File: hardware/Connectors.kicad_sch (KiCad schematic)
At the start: 2 parts, among them J2 Conn_02x20_Odd_Even, U1 AS222-35PN-933

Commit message: minor improvements
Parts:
- added C25: 10pF, Capacitor_SMD:CP_Elec_6.3x7.7, symbol Device:CP_Small
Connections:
- net +24V: now also U1.27, U1.37
- net +5V: now also C25.1
- net AMS: now also U1.31; no longer U1.75
- net BREAK_LIGHT_IN: now also U1.74; no longer U1.93
- net GND: now also U1.10, U1.11, U1.12, U1.13, U1.33, U1.4, U1.44, U1.48, U1.54, U1.75, U1.81, U1.82, U1.83, U1.84, U1.9, C25.2
- net HVD: now also U1.42; no longer U1.74
- net SPARE: now also U1.43; no longer U1.66
- net TD: now also U1.53; no longer U1.76
- net TSMS: now also U1.32; no longer U1.65
- net V_PUMP: now also U1.64, U1.65, U1.66; no longer U1.83, U1.84, U1.85
- new net V_SPARE_1: U1.93
- new net V_SPARE_2: U1.85
- new net V_SPARE_3: U1.76
- no-connect marks 24 -> 5

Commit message: fuck
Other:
- note added: "res ref do wyjbania"
- note added: "ws_rr/rl/fr/fl do wyjbania na jeden"
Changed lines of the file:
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@@
     (effects (font (size 2.9972 2.9972) (thickness 0.5994) bold) (justify right bottom))
+  )
+  (text "ws_rr/rl/fr/fl do wyjbania na jeden" (at -5.08 62.23 0)
+    (effects (font (size 1.27 1.27)) (justify left bottom))
+  )
+  (text "res ref do wyjbania\n" (at 76.2 125.73 0)
+    (effects (font (size 1.27 1.27)) (justify left bottom))
   )
   (text "BUS" (at 136.652 72.39 180)

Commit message: jolo
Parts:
- U1: footprint AS222-35PN-933C:AS222-35PN-933C-ver3-drill_0.72_size_1.02 -> Autosport:AS222-35PN-933C-ver4-drill_0.72_size_1.02
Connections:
- net GND: no longer U1.10, U1.11, U1.12, U1.13, U1.4, U1.9
- net USB_DM: no longer U1.17
- net USB_DP: no longer U1.16
- net DASHBOARD renamed ODRIVE
- net ODRIVE: now also U1.10, U1.9
- net JETSON_??? renamed JETSON
- net WS_RL renamed LAPTIMER
- net WS_RR renamed DASH
- new net TSAL_HV_AIR: U1.16
- new net TSAL_HV_SIG: U1.17
- new net TSAL_LED_GREEN: U1.4
- new net TSAL_LED_HV: U1.12
- new net TSAL_LED_LV: U1.13
- new net TSAL_LED_RED: U1.11

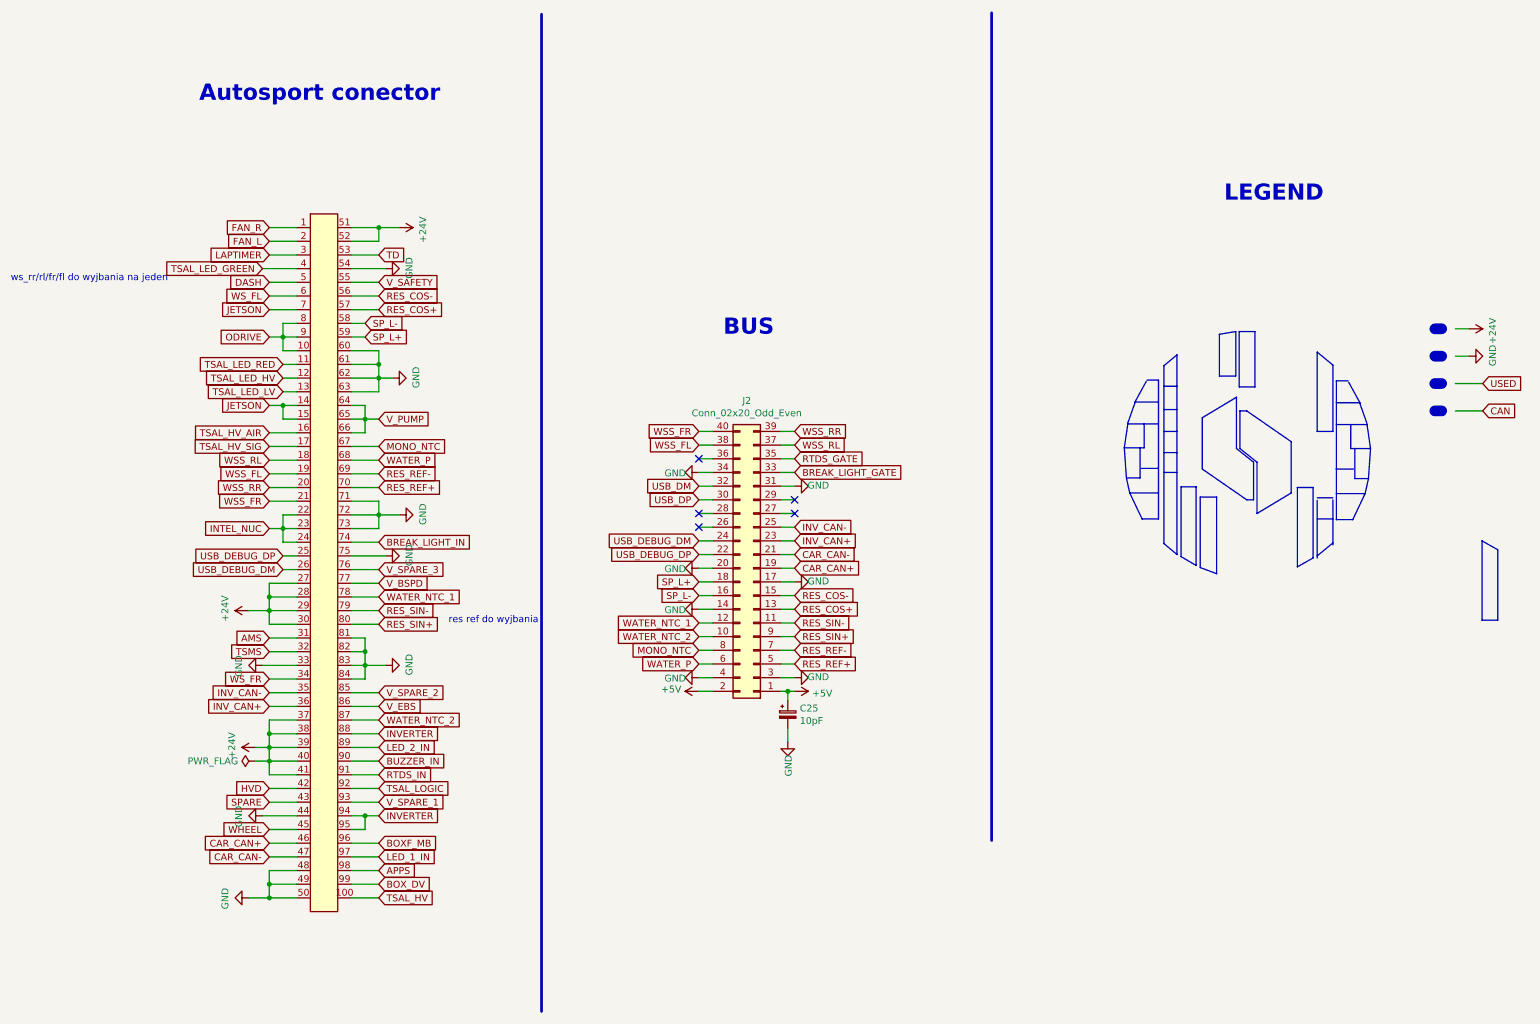
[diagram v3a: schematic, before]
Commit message: currected sf autosport connector, also updated firmware to better handle the showing of board status throught the on board LEDs
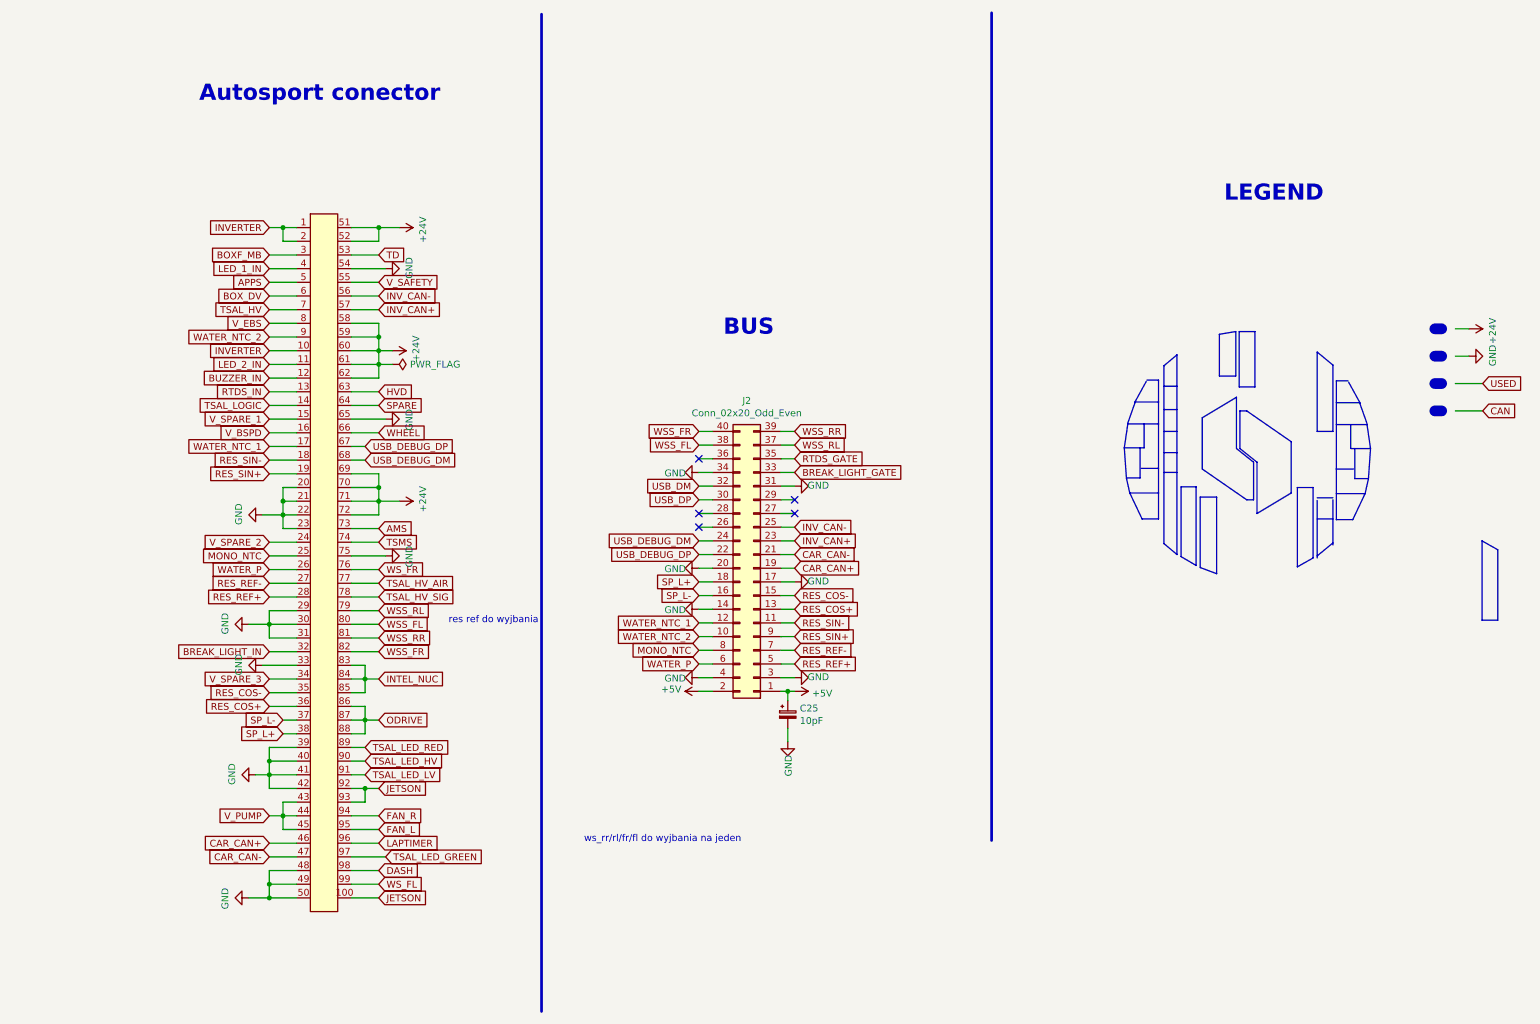
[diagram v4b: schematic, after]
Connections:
- net +24V: now also U1.58, U1.59, U1.60, U1.61, U1.62, U1.69, U1.70, U1.71, U1.72; no longer U1.27, U1.28, U1.29, U1.30, U1.37, U1.38, U1.39, U1.40, U1.41
- net AMS: now also U1.73; no longer U1.31
- net APPS: now also U1.5; no longer U1.98
- net BOXF_MB: now also U1.3; no longer U1.96
- net BOX_DV: now also U1.6; no longer U1.99
- net BREAK_LIGHT_IN: now also U1.32; no longer U1.74
- net BUZZER_IN: now also U1.12; no longer U1.90
- net DASH: now also U1.98; no longer U1.5
- net FAN_L: now also U1.95; no longer U1.2
- net FAN_R: now also U1.94; no longer U1.1
- net GND: now also U1.20, U1.21, U1.22, U1.23, U1.29, U1.30, U1.31, U1.39, U1.40, U1.41, U1.42, U1.65; no longer U1.44, U1.60, U1.61, U1.62, U1.63, U1.71, U1.72, U1.73, U1.81, U1.82, U1.83, U1.84
- net HVD: now also U1.63; no longer U1.42
- net INTEL_NUC: now also U1.83, U1.84, U1.85; no longer U1.22, U1.23, U1.24
- net INVERTER: now also U1.1, U1.10, U1.2; no longer U1.88, U1.94, U1.95
- net INV_CAN+: now also U1.57; no longer U1.36
- net INV_CAN-: now also U1.56; no longer U1.35
- net JETSON: now also U1.100, U1.92, U1.93; no longer U1.14, U1.15, U1.7
- net LAPTIMER: now also U1.96; no longer U1.3
- net LED_1_IN: now also U1.4; no longer U1.97
- net LED_2_IN: now also U1.11; no longer U1.89
- net MONO_NTC: now also U1.25; no longer U1.67
- net ODRIVE: now also U1.86, U1.87, U1.88; no longer U1.10, U1.8, U1.9
- net RES_COS+: now also U1.36; no longer U1.57
- net RES_COS-: now also U1.35; no longer U1.56
- net RES_REF+: now also U1.28; no longer U1.70
- net RES_REF-: now also U1.27; no longer U1.69
- net RES_SIN+: now also U1.19; no longer U1.80
- net RES_SIN-: now also U1.18; no longer U1.79
- net RTDS_IN: now also U1.13; no longer U1.91
- net SPARE: now also U1.64; no longer U1.43
- net SP_L+: now also U1.38; no longer U1.59
- net SP_L-: now also U1.37; no longer U1.58
- net TSAL_HV: now also U1.7; no longer U1.100
- net TSAL_HV_AIR: now also U1.77; no longer U1.16
- net TSAL_HV_SIG: now also U1.78; no longer U1.17
- net TSAL_LED_GREEN: now also U1.97; no longer U1.4
- net TSAL_LED_HV: now also U1.90; no longer U1.12
- net TSAL_LED_LV: now also U1.91; no longer U1.13
- net TSAL_LED_RED: now also U1.89; no longer U1.11
- net TSAL_LOGIC: now also U1.14; no longer U1.92
- net TSMS: now also U1.74; no longer U1.32
- net USB_DEBUG_DM: now also U1.68; no longer U1.26
- net USB_DEBUG_DP: now also U1.67; no longer U1.25
- net V_BSPD: now also U1.16; no longer U1.77
- net V_EBS: now also U1.8; no longer U1.86
- net V_PUMP: now also U1.43, U1.44, U1.45; no longer U1.64, U1.65, U1.66
- net V_SPARE_1: now also U1.15; no longer U1.93
- net V_SPARE_2: now also U1.24; no longer U1.85
- net V_SPARE_3: now also U1.34; no longer U1.76
- net WATER_NTC_1: now also U1.17; no longer U1.78
- net WATER_NTC_2: now also U1.9; no longer U1.87
- net WATER_P: now also U1.26; no longer U1.68
- net WHEEL: now also U1.66; no longer U1.45
- net WSS_FL: now also U1.80; no longer U1.19
- net WSS_FR: now also U1.82; no longer U1.21
- net WSS_RL: now also U1.79; no longer U1.18
- net WSS_RR: now also U1.81; no longer U1.20
- net WS_FL: now also U1.99; no longer U1.6
- net WS_FR: now also U1.76; no longer U1.34

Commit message: major schematic update, changed optocouplers for different, added new fuses for 5v supply for water and potentiometers and 24v supply for BSPD/ESB, updated autosport connector, and some other changes
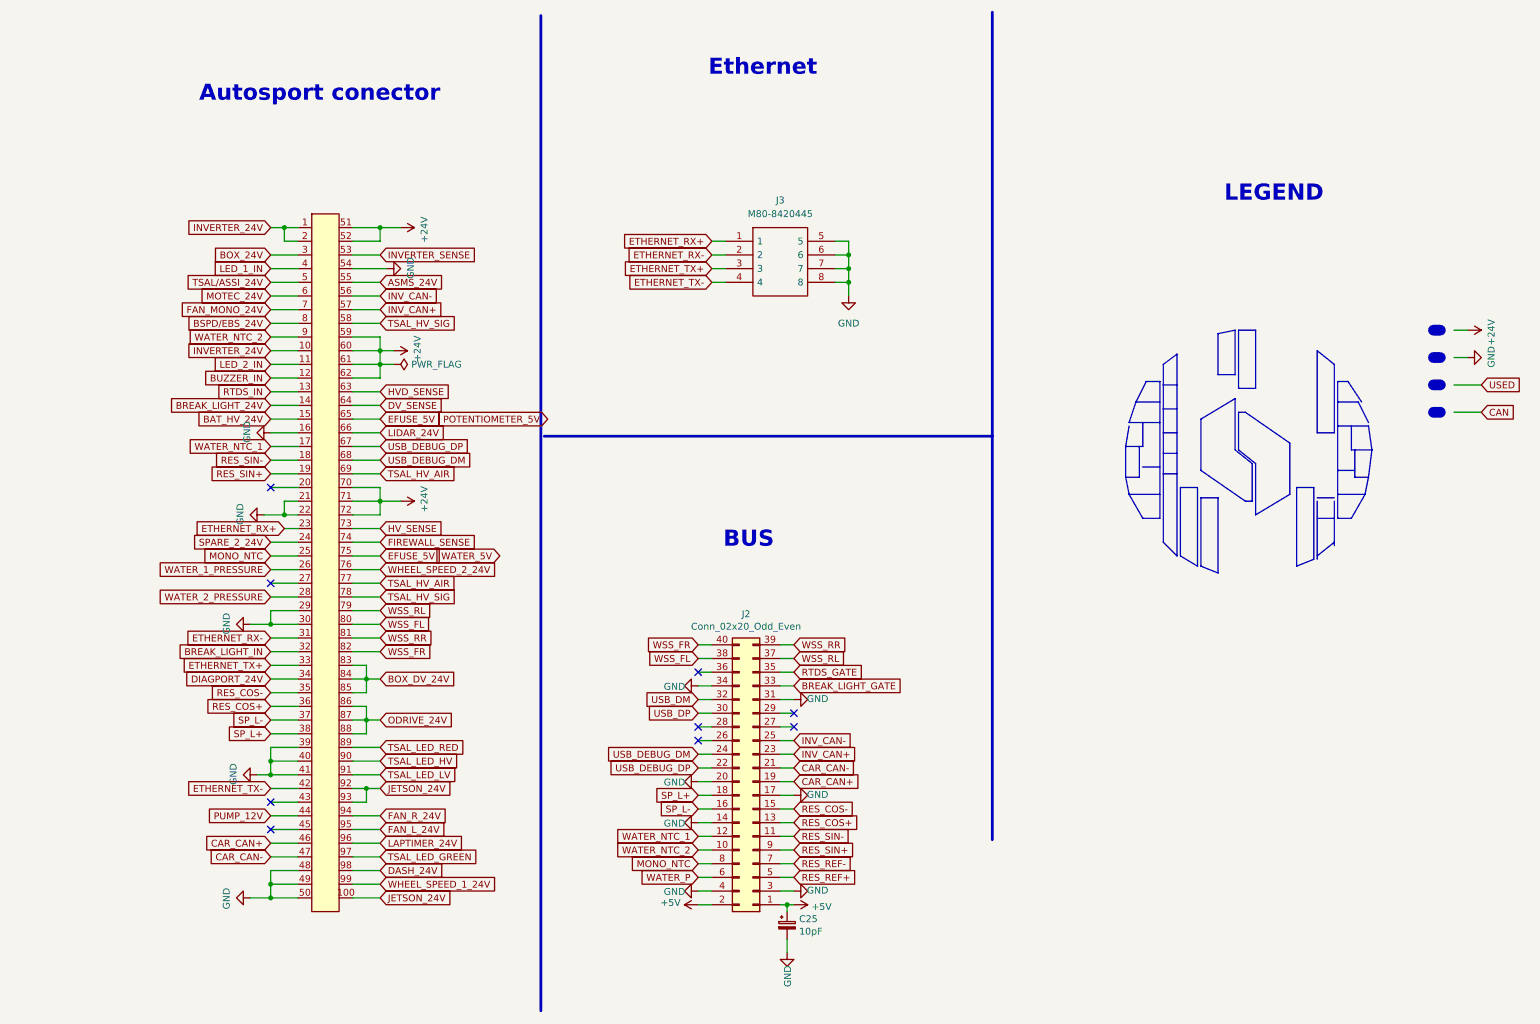
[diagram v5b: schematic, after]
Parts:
- added J3: M80-8420445, M80-8420445, symbol M80-8420445:M80-8420445
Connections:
- net V_BSPD is gone; now on net GND: U1.16
- net +24V: no longer U1.58, U1.69
- net GND: now also J3.5, J3.6, J3.7, J3.8; no longer U1.20, U1.23, U1.31, U1.33, U1.42, U1.65, U1.75
- net RES_REF+: no longer U1.28
- net RES_REF-: no longer U1.27
- net TSAL_HV_AIR: now also U1.69
- net TSAL_HV_SIG: now also U1.58
- net WATER_P: no longer U1.26
- net AMS renamed HV_SENSE
- net APPS renamed TSAL/ASSI_24V
- net BOXF_MB renamed BOX_24V
- net BOX_DV renamed MOTEC_24V
- net DASH renamed DASH_24V
- net FAN_L renamed FAN_L_24V
- net FAN_R renamed FAN_R_24V
- net HVD renamed HVD_SENSE
- net INTEL_NUC renamed BOX_DV_24V
- net INVERTER renamed INVERTER_24V
- net JETSON renamed JETSON_24V
- net LAPTIMER renamed LAPTIMER_24V
- net ODRIVE renamed ODRIVE_24V
- net SPARE renamed DV_SENSE
- net TD renamed INVERTER_SENSE
- net TSAL_HV renamed FAN_MONO_24V
- net TSAL_LOGIC renamed BREAK_LIGHT_24V
- net TSMS renamed FIREWALL_SENSE
- net V_EBS renamed BSPD/EBS_24V
- removed net V_PUMP: U1.43, U1.44, U1.45
- net V_SAFETY renamed ASMS_24V
- net V_SPARE_1 renamed BAT_HV_24V
- net V_SPARE_2 renamed SPARE_2_24V
- net V_SPARE_3 renamed DIAGPORT_24V
- net WHEEL renamed LIDAR_24V
- net WS_FL renamed WHEEL_SPEED_1_24V
- net WS_FR renamed WHEEL_SPEED_2_24V
- new net EFUSE_5V: U1.65, U1.75
- new net ETHERNET_RX+: J3.1, U1.23
- new net ETHERNET_RX-: J3.2, U1.31
- new net ETHERNET_TX+: J3.3, U1.33
- new net ETHERNET_TX-: J3.4, U1.42
- new net PUMP_12V: U1.44
- new net WATER_1_PRESSURE: U1.26
- new net WATER_2_PRESSURE: U1.28
- no-connect marks 5 -> 9
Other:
- note added: "Ethernet"
- note removed: "res ref do wyjbania"
- note removed: "ws_rr/rl/fr/fl do wyjbania na jeden"
- moved on the sheet: C25, J2

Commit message: changed some footprints for clarity, and made some progress on board
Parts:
- added J4: M80-8661022, M80-8661022:M808661022, symbol M80-8661022:M80-8661022
- added R54: R_Small, Resistor_SMD:R_0603_1608Metric, symbol Device:R_Small
- J3: footprint M80-8420445 -> M80-8420445:M80-8420445
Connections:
- net RES_REF- is gone; now on net GND: J2.7 (Pin_7)
- net WATER_P is gone; now on net WATER_1_PRESSURE: J2.6 (Pin_6)
- net +24V: now also J4.9
- net GND: now also J4.10, J4.MH1, J4.MH2, J4.MH3, J4.MH4
- net TSAL_HV_AIR: now also J4.1, J4.7
- net TSAL_HV_SIG: now also J4.6, J4.8
- net TSAL_LED_GREEN: now also J4.2
- net TSAL_LED_HV: now also J4.4
- net TSAL_LED_LV: now also J4.3
- net TSAL_LED_RED: now also J4.5
- net WATER_2_PRESSURE: now also R54.2
- net SPARE_1_24V: now reaches U1.45
- net RES_REF+: no longer names the net of J2.5 (Pin_5)
- net RES_REF+: now also R54.1
- net USB_DM: no longer names the net of J2.32 (Pin_32)
- net USB_DP: no longer names the net of J2.30 (Pin_30)
- no-connect marks 9 -> 10
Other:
- note added: "Tsal"

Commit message: finished new wersion of the board
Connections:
- net +24V: no longer J4.9
- net ETHERNET_RX+: now also J3.2; no longer J3.1
- net ETHERNET_RX-: now also J3.1; no longer J3.2
- net ETHERNET_TX+: now also J3.4; no longer J3.3
- net ETHERNET_TX-: now also J3.3; no longer J3.4
- net GND: now also J4.1; no longer J4.10
- net TSAL_LED_GREEN: now also J4.5; no longer J4.2
- net TSAL_LED_RED: now also J4.4; no longer J4.5
- net SPARE_1_SENSE: now reaches U1.20
- net SPARE_2_SENSE: now reaches U1.27
- net SPARE_3_SENSE: now reaches U1.43
- removed net TSAL_HV_AIR: J4.1, J4.7, U1.69, U1.77
- net TSAL_HV_SIG renamed TSAL_HV_INV_SIG
- net TSAL_HV_INV_SIG: no longer J4.6, U1.78
- net TSAL_LED_HV renamed TSAL_DASH_LED_RED
- net TSAL_DASH_LED_RED: now also J4.2; no longer J4.4
- net TSAL_LED_LV renamed TSAL_DASH_LED_GREEN
- new net TSAL_24V: J4.9
- new net TSAL_HV_AIR1: J4.6, U1.69
- new net TSAL_HV_AIR2: J4.10, U1.77
- new net TSAL_HV_BAT_SIG: J4.7, U1.78
- no-connect marks 10 -> 7

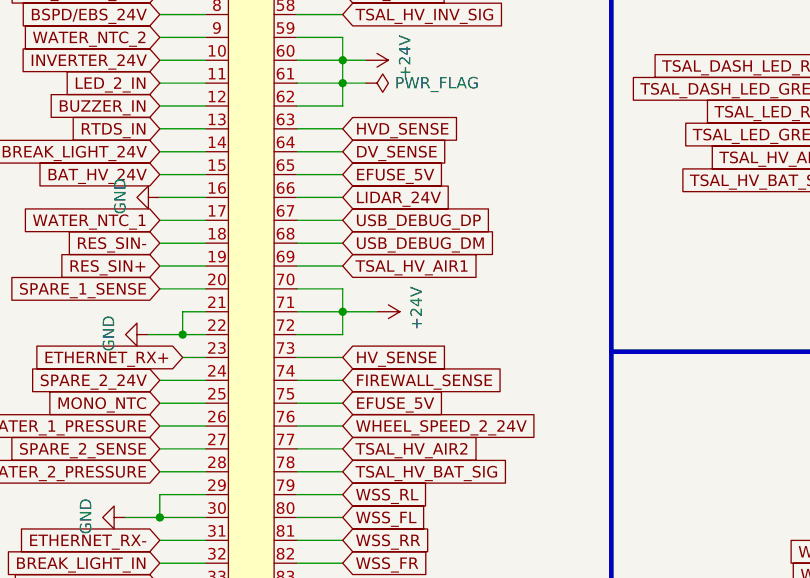
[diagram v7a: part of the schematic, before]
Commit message: debuged the board, changed one opto for mosfet, changed the way water and potentiometers were supplied. Also standrised opamps (yoinked opamps from data Data_Acquisition_Cards)
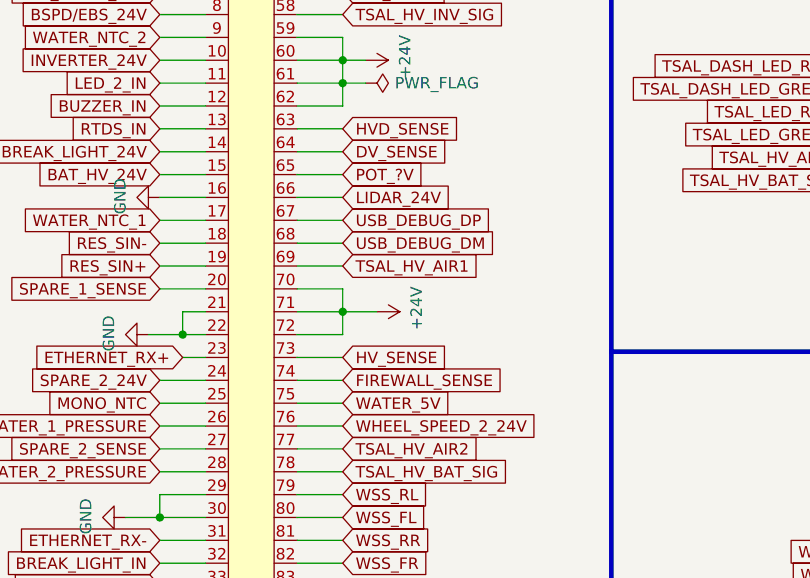
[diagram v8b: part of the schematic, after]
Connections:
- net EFUSE_5V renamed POT_?V
- net POT_?V: no longer U1.75
- new net WATER_5V: U1.75
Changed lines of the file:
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@@
     )
   )
-  (global_label "EFUSE_5V" (shape input) (at 63.5 113.03 0) (fields_autoplaced)
+  (global_label "WATER_5V" (shape input) (at 63.5 113.03 0) (fields_autoplaced)
     (effects (font (size 1.27 1.27)) (justify left))
     (property "Intersheet References" "${INTERSHEET_REFS}" (id 0) (at 75.0166 112.9506 0)
@@
     )
   )
-  (global_label "EFUSE_5V" (shape input) (at 63.5 87.63 0) (fields_autoplaced)
-    (effects (font (size 1.27 1.27)) (justify left))
-    (property "Intersheet References" "${INTERSHEET_REFS}" (id 0) (at 75.0166 87.5506 0)
+  (global_label "POT_?V" (shape input) (at 63.5 87.63 0) (fields_autoplaced)
+    (effects (font (size 1.27 1.27)) (justify left))
+    (property "Intersheet References" "${INTERSHEET_REFS}" (id 0) (at 72.5371 87.5506 0)
       (effects (font (size 1.27 1.27)) (justify left) hide)
     )
@@
   (symbol (lib_id "power:GND") (at 121.92 90.805 0) (unit 1)
     (in_bom yes) (on_board yes) (fields_autoplaced)
-    (property "Reference" "#PWR?" (id 0) (at 121.92 97.155 0)
-      (effects (font (size 1.27 1.27)) hide)
-    )
+    (property "Reference" "#PWR0153" (id 0) (at 121.92 97.155 0)
+      (effects (font (size 1.27 1.27)) hide)
+    )
